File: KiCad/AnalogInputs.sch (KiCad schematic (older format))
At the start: 0 parts

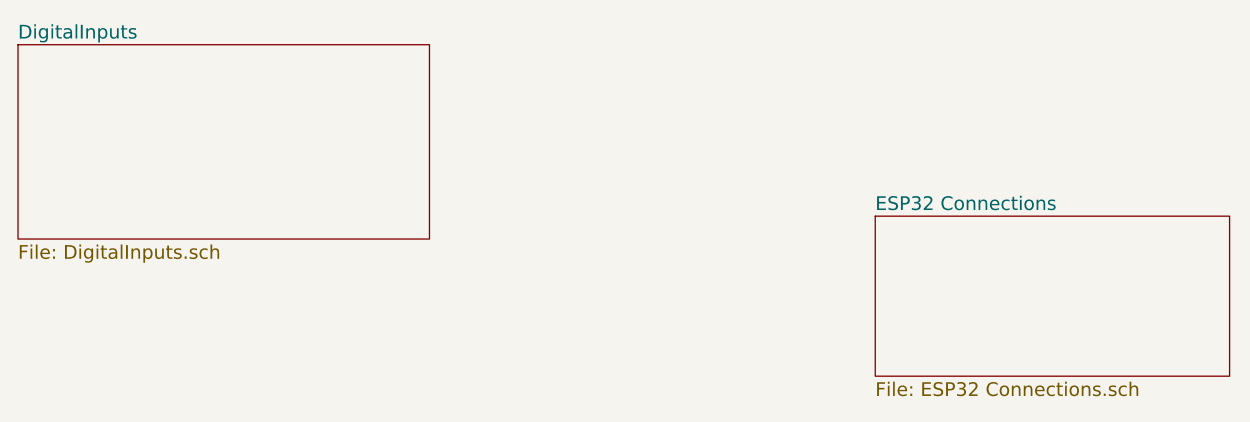
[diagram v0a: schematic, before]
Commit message: Split into separate schemas
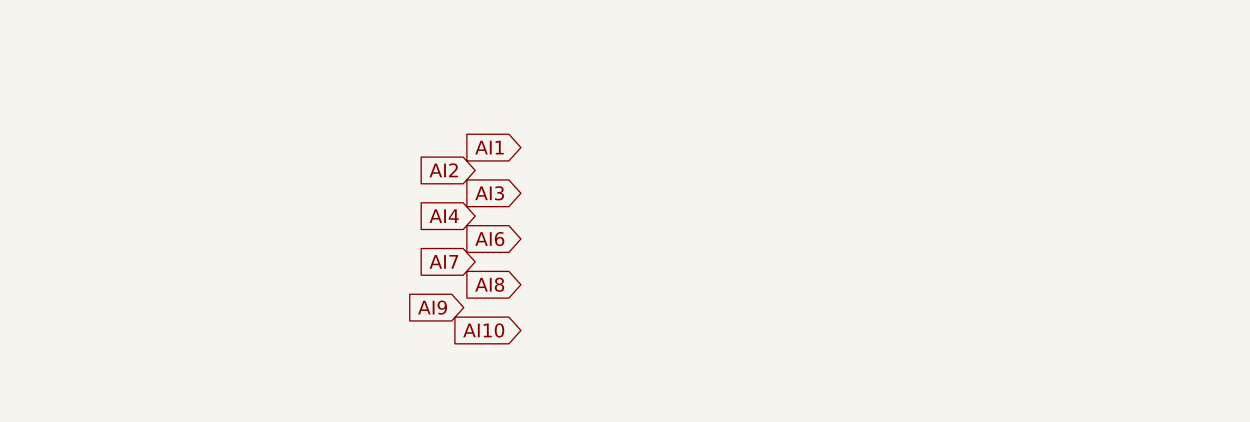
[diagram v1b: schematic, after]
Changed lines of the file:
@@
 $Descr A4 11693 8268
 encoding utf-8
-Sheet 1 3
+Sheet 4 4
 Title ""
 Date ""
@@
 Comment4 ""
 $EndDescr
-$Sheet
-S 1350 2150 1800 850
-U 591810E7
-F0 "DigitalInputs" 60
-F1 "DigitalInputs.sch" 60
-$EndSheet
-$Sheet
-S 5100 2900 1550 700
-U 59181FE5
-F0 "ESP32 Connections" 60
-F1 "ESP32 Connections.sch" 60
-$EndSheet
+Text GLabel 3550 2600 0    60   Input ~ 0
+AI1
+Text GLabel 3350 2700 0    60   Input ~ 0
+AI2
+Text GLabel 3550 2800 0    60   Input ~ 0
+AI3
+Text GLabel 3350 2900 0    60   Input ~ 0
+AI4
+Text GLabel 3550 3000 0    60   Input ~ 0
+AI6
+Text GLabel 3350 3100 0    60   Input ~ 0
+AI7
+Text GLabel 3550 3200 0    60   Input ~ 0
+AI8
+Text GLabel 3300 3300 0    60   Input ~ 0
+AI9
+Text GLabel 3550 3400 0    60   Input ~ 0
+AI10
 $EndSCHEMATC
